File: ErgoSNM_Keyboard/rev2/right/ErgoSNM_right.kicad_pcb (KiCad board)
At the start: 2 copper layers, 115.6 x 106.7 mm, 111 parts, among them J1 USB_C_Receptacle_USB2.0, J2 USB_C_Receptacle_USB2.0, J3 PJ-393_TRRS_8P, J4 Conn_01x08, SW1 BOOT, SW2 RESET, U1 RT9013-33GB, U2 SRV05-4, U3 W25Q128JVS, U4 RP2040, Y1 12MHz

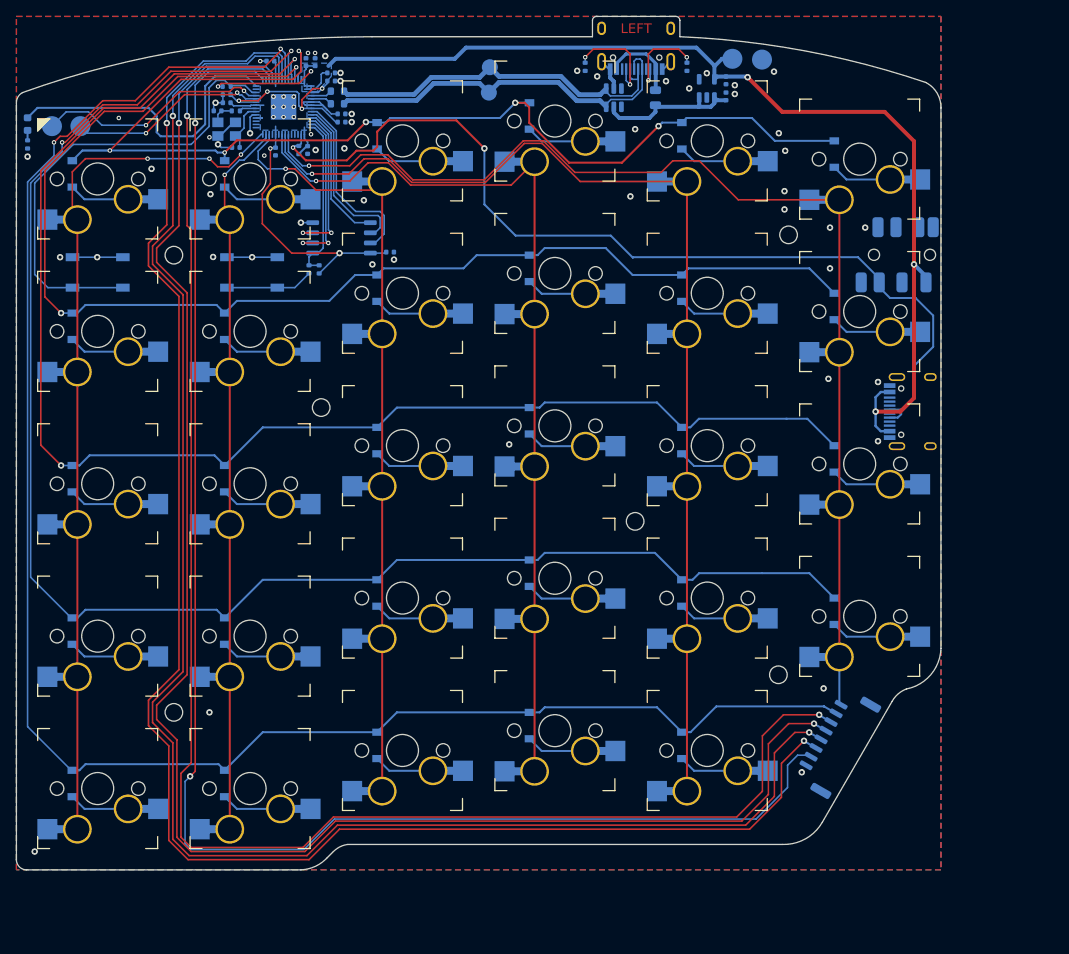
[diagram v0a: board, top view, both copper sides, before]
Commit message: Update right hand schematic
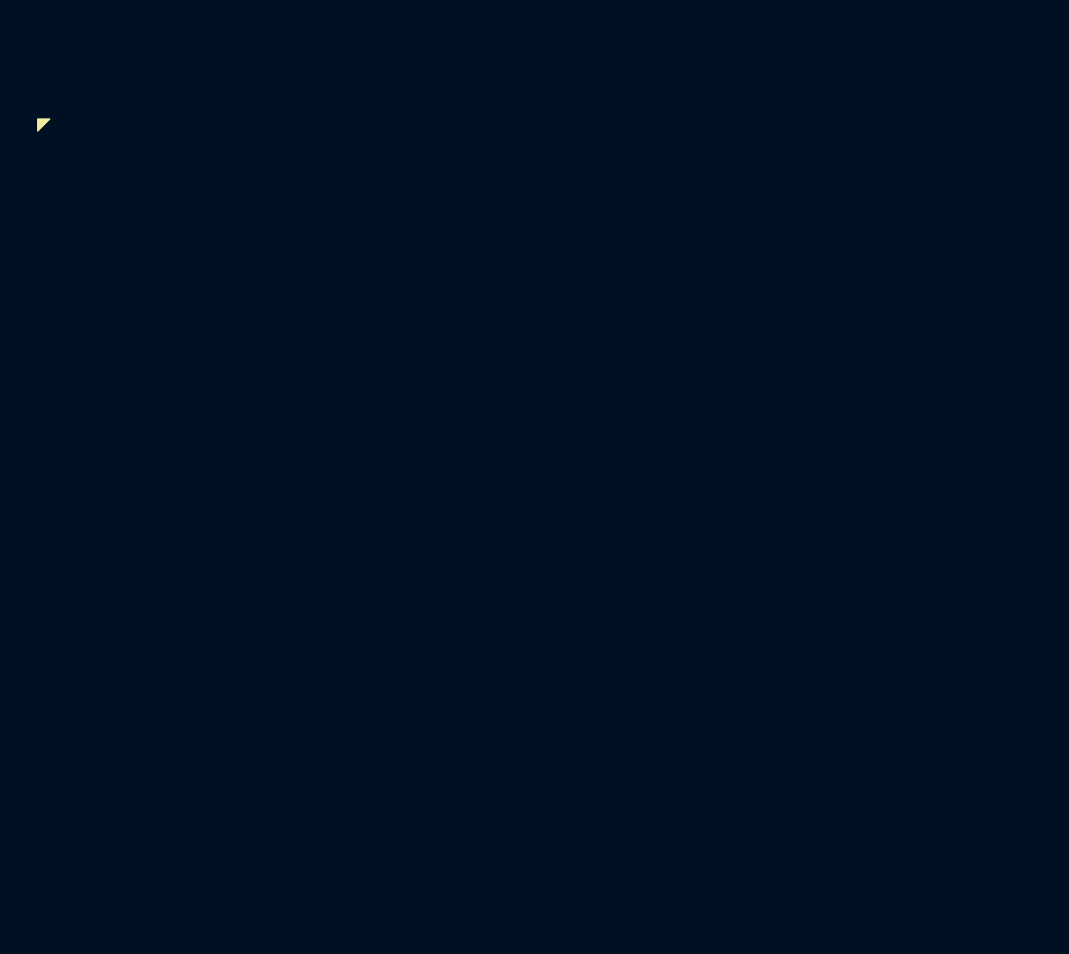
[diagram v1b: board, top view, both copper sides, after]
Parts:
- removed C1, C16, C2, C8: 1uF, Capacitor_SMD:C_0402_1005Metric
- removed C10, C11, C12, C13, C14, C15, C3, C6, C7, C9: 100nF, Capacitor_SMD:C_0402_1005Metric
- removed C4, C5: 20pF, Capacitor_SMD:C_0402_1005Metric
- removed D1, D10, D11, D12, D13, D14, D15, D16, D17, D18, D19, D2, D20, D21, D22, D23, D24, D25, D26, D27, D28, D29, D3, D4, D5, D6, D7, D8, D9: 1N4148, Diode_SMD:D_SOD-123
- removed F1: 500mA, 6V, Fuse:Fuse_0805_2012Metric
- removed G***: LOGO, LOGO
- removed H1, H2, H3, H4, H5, H6: MountingHole, MountingHole:MountingHole_2.2mm_M2
- removed J1, J2: USB_C_Receptacle_USB2.0, Connector_USB:USB_C_Receptacle_HRO_TYPE-C-31-M-12
- removed J3: PJ-393_TRRS_8P, ErgoSNM_Keyboard:PJ-393 8P TRRS
- removed J4: Conn_01x08, Connector_JST:JST_GH_SM08B-GHS-TB_1x08-1MP_P1.25mm_Horizontal
- removed KEY1, KEY10, KEY11, KEY12, KEY13, KEY14, KEY15, KEY16, KEY17, KEY18, KEY19, KEY2, KEY20, KEY21, KEY22, KEY23, KEY24, KEY25, KEY26, KEY27, KEY28, KEY29, KEY3, KEY4, KEY5, KEY6, KEY7, KEY8, KEY9: SW_Push_45deg, key-switches:MX_switch_PTH_hotswap_A
- removed LD1: Red, LED_SMD:LED_0603_1608Metric
- removed R1, R2, R4: 5.1k, Resistor_SMD:R_0402_1005Metric
- removed R10, R8: 10k, Resistor_SMD:R_0402_1005Metric
- removed R3, R7, R9: 1k, Resistor_SMD:R_0402_1005Metric
- removed R5, R6: 27, Resistor_SMD:R_0603_1608Metric
- removed SW1: BOOT, Button_Switch_SMD:SW_SPST_TL3342
- removed SW2: RESET, Button_Switch_SMD:SW_SPST_TL3342
- removed TP1, TP4, TP5, TP6: TestPoint, TestPoint:TestPoint_Pad_D2.5mm
- removed TP2, TP3: TestPoint, TestPoint:TestPoint_Pad_D2.0mm
- removed U1: RT9013-33GB, Package_TO_SOT_SMD:SOT-23-5
- removed U2: SRV05-4, Package_TO_SOT_SMD:SOT-23-6
- removed U3: W25Q128JVS, Package_SO:SOIC-8_5.23x5.23mm_P1.27mm
- removed U4: RP2040, Package_DFN_QFN:QFN-56-1EP_7x7mm_P0.4mm_EP3.2x3.2mm
- removed Y1: 12MHz, Crystal:Crystal_SMD_3225-4Pin_3.2x2.5mm
- removed kibuzzard-63A148C1: G***, kibuzzard-63A148C1
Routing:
- net ROW_4: track 221.8 -> 0.00 mm, vias 2 -> 0
- net Encoder_A: track 208.6 -> 0.00 mm, vias 2 -> 0
- net COL_6: track 208.1 -> 0.00 mm, vias 2 -> 0
- net +3V3: track 207.8 -> 0.00 mm, vias 7 -> 0
- net COL_7: track 205.0 -> 0.00 mm, vias 2 -> 0
- net ROW_3: track 202.9 -> 0.00 mm, vias 2 -> 0
- net ROW_5: track 199.4 -> 0.00 mm, vias 2 -> 0
- net Encoder_B: track 190.0 -> 0.00 mm, vias 2 -> 0
- net ROW_2: track 182.3 -> 0.00 mm, vias 2 -> 0
- net ROW_1: track 160.9 -> 0.00 mm, vias 2 -> 0
- net ROW_0: track 146.9 -> 0.00 mm, vias 6 -> 0
- net COL_5: track 143.1 -> 0.00 mm, vias 1 -> 0
- net COL_4: track 135.8 -> 0.00 mm, vias 1 -> 0
- net SERIAL: track 118.2 -> 0.00 mm, vias 2 -> 0
- net COL_3: track 114.8 -> 0.00 mm, vias 1 -> 0
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- removed copper zone on B.Cu, net +3V3
- removed copper zone on B.Cu, net GND
- removed copper zone on F.Cu, net GND
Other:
- board outline removed
- board text removed: "LEFT"

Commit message: Update right PCB
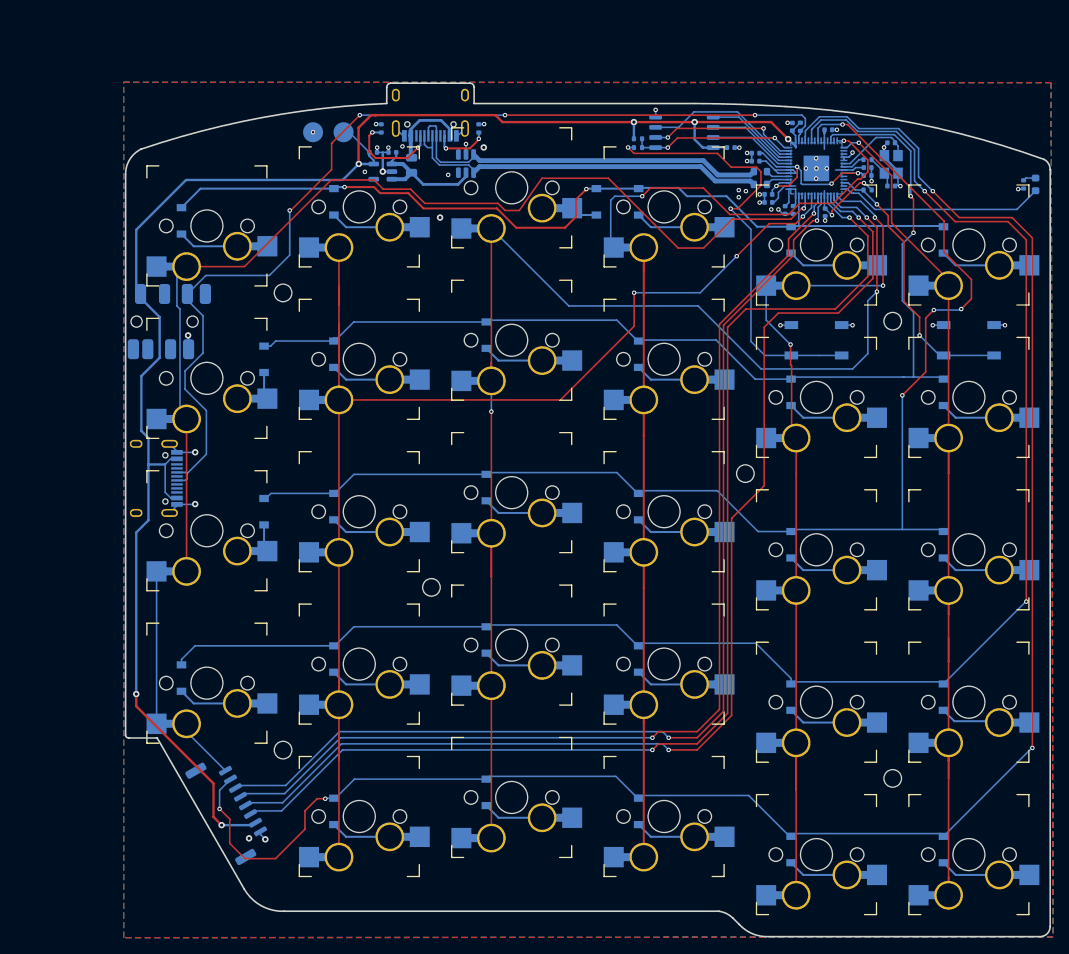
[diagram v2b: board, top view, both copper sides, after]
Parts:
- added C1: 1uF, Capacitor_SMD:C_0402_1005Metric, B.Cu at (108.0, 42.4)
- added C10: 100nF, Capacitor_SMD:C_0402_1005Metric, B.Cu at (162.5, 39.6)
- added C11: 100nF, Capacitor_SMD:C_0402_1005Metric, B.Cu at (167.4, 44.3)
- added C12: 100nF, Capacitor_SMD:C_0402_1005Metric, B.Cu at (162.1, 49.9)
- added C13: 100nF, Capacitor_SMD:C_0402_1005Metric, B.Cu at (158.1, 49.6)
- added C14: 100nF, Capacitor_SMD:C_0402_1005Metric, B.Cu at (157.1, 49.6)
- added C15: 100nF, Capacitor_SMD:C_0402_1005Metric, B.Cu at (153.4, 43.5)
- added C16: 1uF, Capacitor_SMD:C_0402_1005Metric, B.Cu at (155.0, 48.6)
- added C2: 1uF, Capacitor_SMD:C_0402_1005Metric, B.Cu at (105.6, 42.4)
- added C3: 100nF, Capacitor_SMD:C_0402_1005Metric, B.Cu at (150.3, 41.8)
- added C4: 20pF, Capacitor_SMD:C_0402_1005Metric, B.Cu at (170.3, 41.2)
- added C5: 20pF, Capacitor_SMD:C_0402_1005Metric, B.Cu at (170.3, 46.6)
- added C6: 100nF, Capacitor_SMD:C_0402_1005Metric, B.Cu at (167.4, 45.3)
- added C7: 100nF, Capacitor_SMD:C_0402_1005Metric, B.Cu at (153.4, 42.5)
- added C8: 1uF, Capacitor_SMD:C_0402_1005Metric, B.Cu at (155.0, 47.6)
- added C9: 100nF, Capacitor_SMD:C_0402_1005Metric, B.Cu at (158.0, 39.2)
- added D1: 1N4148, Diode_SMD:D_SOD-123, B.Cu at (176.8, 53.3)
- added D10: 1N4148, Diode_SMD:D_SOD-123, B.Cu at (119.7, 65.2)
- added D11: 1N4148, Diode_SMD:D_SOD-123, B.Cu at (100.6, 67.6)
- added D12: 1N4148, Diode_SMD:D_SOD-123, B.Cu at (91.9, 68.3)
- added D13: 1N4148, Diode_SMD:D_SOD-123, B.Cu at (176.8, 91.4)
- added D14: 1N4148, Diode_SMD:D_SOD-123, B.Cu at (157.8, 91.4)
- added D15: 1N4148, Diode_SMD:D_SOD-123, B.Cu at (138.7, 86.7)
- added D16: 1N4148, Diode_SMD:D_SOD-123, B.Cu at (119.7, 84.3)
- added D17: 1N4148, Diode_SMD:D_SOD-123, B.Cu at (100.6, 86.7)
- added D18: 1N4148, Diode_SMD:D_SOD-123, B.Cu at (91.9, 87.3)
- added D19: 1N4148, Diode_SMD:D_SOD-123, B.Cu at (176.8, 110.5)
- added D2: 1N4148, Diode_SMD:D_SOD-123, B.Cu at (157.8, 53.3)
- added D20: 1N4148, Diode_SMD:D_SOD-123, B.Cu at (157.8, 110.5)
- added D21: 1N4148, Diode_SMD:D_SOD-123, B.Cu at (138.7, 105.7)
- added D22: 1N4148, Diode_SMD:D_SOD-123, B.Cu at (119.7, 103.3)
- added D23: 1N4148, Diode_SMD:D_SOD-123, B.Cu at (100.6, 105.7)
- added D24: 1N4148, Diode_SMD:D_SOD-123, B.Cu at (81.6, 108.1)
- added D25: 1N4148, Diode_SMD:D_SOD-123, B.Cu at (176.8, 129.5)
- added D26: 1N4148, Diode_SMD:D_SOD-123, B.Cu at (157.8, 129.5)
- added D27: 1N4148, Diode_SMD:D_SOD-123, B.Cu at (138.7, 124.8)
- added D28: 1N4148, Diode_SMD:D_SOD-123, B.Cu at (119.7, 122.4)
- added D29: 1N4148, Diode_SMD:D_SOD-123, B.Cu at (100.6, 124.8)
- added D3: 1N4148, Diode_SMD:D_SOD-123, B.Cu at (138.7, 48.6)
- added D4: 1N4148, Diode_SMD:D_SOD-123, B.Cu at (133.5, 48.6)
- added D5: 1N4148, Diode_SMD:D_SOD-123, B.Cu at (100.6, 48.6)
- added D6: 1N4148, Diode_SMD:D_SOD-123, B.Cu at (81.6, 51.0)
- added D7: 1N4148, Diode_SMD:D_SOD-123, B.Cu at (176.8, 72.4)
- added D8: 1N4148, Diode_SMD:D_SOD-123, B.Cu at (157.8, 72.4)
- added D9: 1N4148, Diode_SMD:D_SOD-123, B.Cu at (138.7, 67.6)
- added F1: 500mA, 6V, Fuse:Fuse_0805_2012Metric, B.Cu at (110.4, 44.0)
- added H1: MountingHole, MountingHole:MountingHole_2.2mm_M2, F.Cu at (152.1, 82.5)
- added H2: MountingHole, MountingHole:MountingHole_2.2mm_M2, F.Cu at (170.5, 120.7)
- added H3: MountingHole, MountingHole:MountingHole_2.2mm_M2, F.Cu at (112.8, 96.8)
- added H4: MountingHole, MountingHole:MountingHole_2.2mm_M2, F.Cu at (170.5, 63.5)
- added H5: MountingHole, MountingHole:MountingHole_2.2mm_M2, F.Cu at (94.3, 60.0)
- added H6: MountingHole, MountingHole:MountingHole_2.2mm_M2, F.Cu at (94.3, 117.1)
- added J1: USB_C_Receptacle_USB2.0, Connector_USB:USB_C_Receptacle_HRO_TYPE-C-31-M-12, B.Cu at (112.7, 36.3)
- added J2: USB_C_Receptacle_USB2.0, Connector_USB:USB_C_Receptacle_HRO_TYPE-C-31-M-12, B.Cu at (77.0, 83.2)
- added J3: PJ-393_TRRS_8P, ErgoSNM_Keyboard:PJ-393 8P TRRS, B.Cu at (79.3, 63.6)
- added J4: Conn_01x08, Connector_JST:JST_GH_SM08B-GHS-TB_1x08-1MP_P1.25mm_Horizontal, B.Cu at (87.7, 124.4)
- added KEY1: SW_Push_45deg, key-switches:MX_switch_PTH_hotswap_A, F.Cu at (180.0, 54.0)
- added KEY10: SW_Push_45deg, key-switches:MX_switch_PTH_hotswap_A, F.Cu at (122.9, 65.9)
- added KEY11: SW_Push_45deg, key-switches:MX_switch_PTH_hotswap_A, F.Cu at (103.8, 68.3)
- added KEY12: SW_Push_45deg, key-switches:MX_switch_PTH_hotswap_A, F.Cu at (84.8, 70.6)
- added KEY13: SW_Push_45deg, key-switches:MX_switch_PTH_hotswap_A, F.Cu at (180.0, 92.1)
- added KEY14: SW_Push_45deg, key-switches:MX_switch_PTH_hotswap_A, F.Cu at (161.0, 92.1)
- added KEY15: SW_Push_45deg, key-switches:MX_switch_PTH_hotswap_A, F.Cu at (141.9, 87.3)
- added KEY16: SW_Push_45deg, key-switches:MX_switch_PTH_hotswap_A, F.Cu at (122.9, 84.9)
- added KEY17: SW_Push_45deg, key-switches:MX_switch_PTH_hotswap_A, F.Cu at (103.8, 87.3)
- added KEY18: SW_Push_45deg, key-switches:MX_switch_PTH_hotswap_A, F.Cu at (84.8, 89.7)
- added KEY19: SW_Push_45deg, key-switches:MX_switch_PTH_hotswap_A, F.Cu at (180.0, 111.1)
- added KEY2: SW_Push_45deg, key-switches:MX_switch_PTH_hotswap_A, F.Cu at (161.0, 54.0)
- added KEY20: SW_Push_45deg, key-switches:MX_switch_PTH_hotswap_A, F.Cu at (161.0, 111.1)
- added KEY21: SW_Push_45deg, key-switches:MX_switch_PTH_hotswap_A, F.Cu at (141.9, 106.4)
- added KEY22: SW_Push_45deg, key-switches:MX_switch_PTH_hotswap_A, F.Cu at (122.9, 104.0)
- added KEY23: SW_Push_45deg, key-switches:MX_switch_PTH_hotswap_A, F.Cu at (103.8, 106.4)
- added KEY24: SW_Push_45deg, key-switches:MX_switch_PTH_hotswap_A, F.Cu at (84.8, 108.7)
- added KEY25: SW_Push_45deg, key-switches:MX_switch_PTH_hotswap_A, F.Cu at (180.0, 130.2)
- added KEY26: SW_Push_45deg, key-switches:MX_switch_PTH_hotswap_A, F.Cu at (161.0, 130.2)
- added KEY27: SW_Push_45deg, key-switches:MX_switch_PTH_hotswap_A, F.Cu at (141.9, 125.4)
- added KEY28: SW_Push_45deg, key-switches:MX_switch_PTH_hotswap_A, F.Cu at (122.9, 123.0)
- added KEY29: SW_Push_45deg, key-switches:MX_switch_PTH_hotswap_A, F.Cu at (103.8, 125.4)
- added KEY3: SW_Push_45deg, key-switches:MX_switch_PTH_hotswap_A, F.Cu at (141.9, 49.2)
- added KEY4: SW_Push_45deg, key-switches:MX_switch_PTH_hotswap_A, F.Cu at (122.9, 46.8)
- added KEY5: SW_Push_45deg, key-switches:MX_switch_PTH_hotswap_A, F.Cu at (103.8, 49.2)
- added KEY6: SW_Push_45deg, key-switches:MX_switch_PTH_hotswap_A, F.Cu at (84.8, 51.6)
- added KEY7: SW_Push_45deg, key-switches:MX_switch_PTH_hotswap_A, F.Cu at (180.0, 73.0)
- added KEY8: SW_Push_45deg, key-switches:MX_switch_PTH_hotswap_A, F.Cu at (161.0, 73.0)
- added KEY9: SW_Push_45deg, key-switches:MX_switch_PTH_hotswap_A, F.Cu at (141.9, 68.3)
- added LD1: Red, LED_SMD:LED_0603_1608Metric, B.Cu at (188.4, 46.4)
- added R1: 5.1k, Resistor_SMD:R_0402_1005Metric, B.Cu at (106.6, 39.4)
- added R10: 10k, Resistor_SMD:R_0402_1005Metric, B.Cu at (167.4, 47.1)
- added R2: 5.1k, Resistor_SMD:R_0402_1005Metric, B.Cu at (118.8, 39.4)
- added R3: 1k, Resistor_SMD:R_0402_1005Metric, B.Cu at (186.9, 46.4)
- added R4: 5.1k, Resistor_SMD:R_0402_1005Metric, B.Cu at (159.0, 39.2)
- added R5: 27, Resistor_SMD:R_0603_1608Metric, B.Cu at (154.0, 44.8)
- added R6: 27, Resistor_SMD:R_0603_1608Metric, B.Cu at (154.0, 46.4)
- added R7: 1k, Resistor_SMD:R_0402_1005Metric, B.Cu at (138.7, 41.8)
- added R8: 10k, Resistor_SMD:R_0402_1005Metric, B.Cu at (138.7, 40.7)
- added R9: 1k, Resistor_SMD:R_0402_1005Metric, B.Cu at (167.4, 43.3)
- added SW1: BOOT, Button_Switch_SMD:SW_SPST_TL3342, B.Cu at (161.0, 65.9)
- added SW2: RESET, Button_Switch_SMD:SW_SPST_TL3342, B.Cu at (180.0, 65.9)
- added TP1: TestPoint, TestPoint:TestPoint_Pad_D2.5mm, B.Cu at (101.9, 39.9)
- added TP4: TestPoint, TestPoint:TestPoint_Pad_D2.5mm, B.Cu at (98.0, 39.9)
- added U1: RT9013-33GB, Package_TO_SOT_SMD:SOT-23-5, B.Cu at (106.8, 44.8)
- added U2: SRV05-4, Package_TO_SOT_SMD:SOT-23-6, B.Cu at (117.2, 43.8)
- added U3: W25Q128JVS, Package_SO:SOIC-8_5.23x5.23mm_P1.27mm, B.Cu at (144.5, 39.9)
- added U4: RP2040, Package_DFN_QFN:QFN-56-1EP_7x7mm_P0.4mm_EP3.2x3.2mm, B.Cu at (161.0, 44.4)
- added Y1: 12MHz, Crystal:Crystal_SMD_3225-4Pin_3.2x2.5mm, B.Cu at (170.3, 43.9)
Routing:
- net +3V3: track 0.00 -> 244.0 mm, vias 0 -> 8
- net ROW_4: track 0.00 -> 227.2 mm, vias 0 -> 4
- net ROW_3: track 0.00 -> 198.9 mm, vias 0 -> 2
- net COL_3: track 0.00 -> 184.8 mm, vias 0 -> 3
- net COL_4: track 0.00 -> 183.8 mm, vias 0 -> 3
- net COL_2: track 0.00 -> 181.7 mm, vias 0 -> 2
- net COL_5: track 0.00 -> 173.8 mm, vias 0 -> 1
- net ROW_2: track 0.00 -> 159.9 mm, vias 0 -> 4
- net ~{CS}: track 0.00 -> 146.0 mm, vias 0 -> 2
- net MISO: track 0.00 -> 145.8 mm, vias 0 -> 2
- net COL_0: track 0.00 -> 143.0 mm, vias 0 -> 1
- net COL_1: track 0.00 -> 139.1 mm, vias 0 -> 3
- net SCLK: track 0.00 -> 135.4 mm, vias 0 -> 2
- net MOSI: track 0.00 -> 133.7 mm, vias 0 -> 2
- net ROW_1: track 0.00 -> 131.8 mm, vias 0 -> 2
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- added copper zone on B.Cu, net +3V3
- added copper zone on B.Cu, net GND
- added copper zone on F.Cu, net GND
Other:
- board outline added: 115.6 x 106.7 mm

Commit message: Update silk and logo
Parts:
- added G***: LOGO, LOGO, B.Cu at (160.9, 122.4)
- added kibuzzard-63A148C1: G***, kibuzzard-63A148C1, B.Cu at (183.4, 124.5)
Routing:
- net COL_2: track 181.7 -> 172.4 mm, vias 2 -> 1
- net ROW_4: track 227.2 -> 232.1 mm
- net SERIAL: track 124.6 -> 121.8 mm
- net /RP2040/BOOT: track 55.0 -> 53.6 mm
- net GND: track 47.7 -> 46.7 mm, vias 45 -> 55
- net COL_4: track 183.8 -> 184.3 mm
- net COL_5: track 173.8 -> 173.4 mm, vias 1 -> 2
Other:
- board text added: "RIGHT"
